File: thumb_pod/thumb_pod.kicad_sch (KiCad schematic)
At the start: 41 parts, among them J1 Conn_02x06_Odd_Even, J2 Conn_02x06_Odd_Even, J3 Conn_02x06_Odd_Even, SW1 SW_Push, SW10 SW_Push, SW2 SW_Push, SW3 SW_Push, SW4 SW_Push, SW5 SW_Push, SW6 SW_Push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

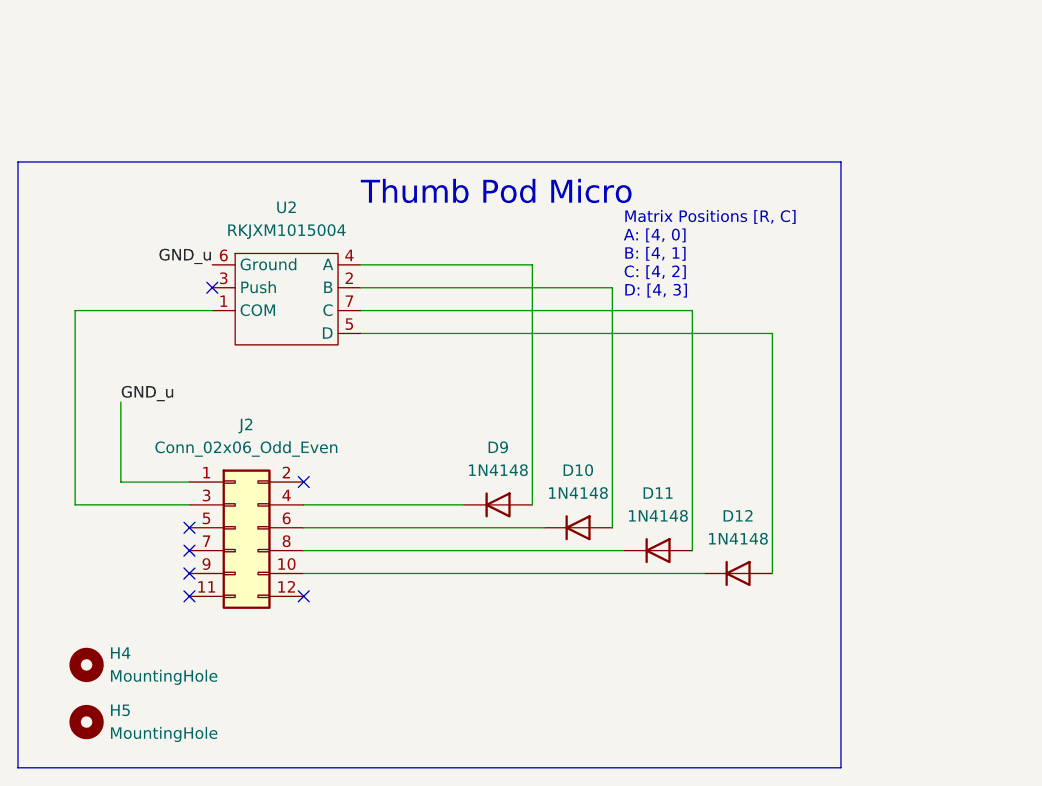
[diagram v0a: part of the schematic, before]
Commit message: - Removed "micro" thumb pod  - Added kailh gm microswitch footprint  - Switch to kail gm microswitches for the "mini" thumb pod  - Reduced size of joystick silkscreen
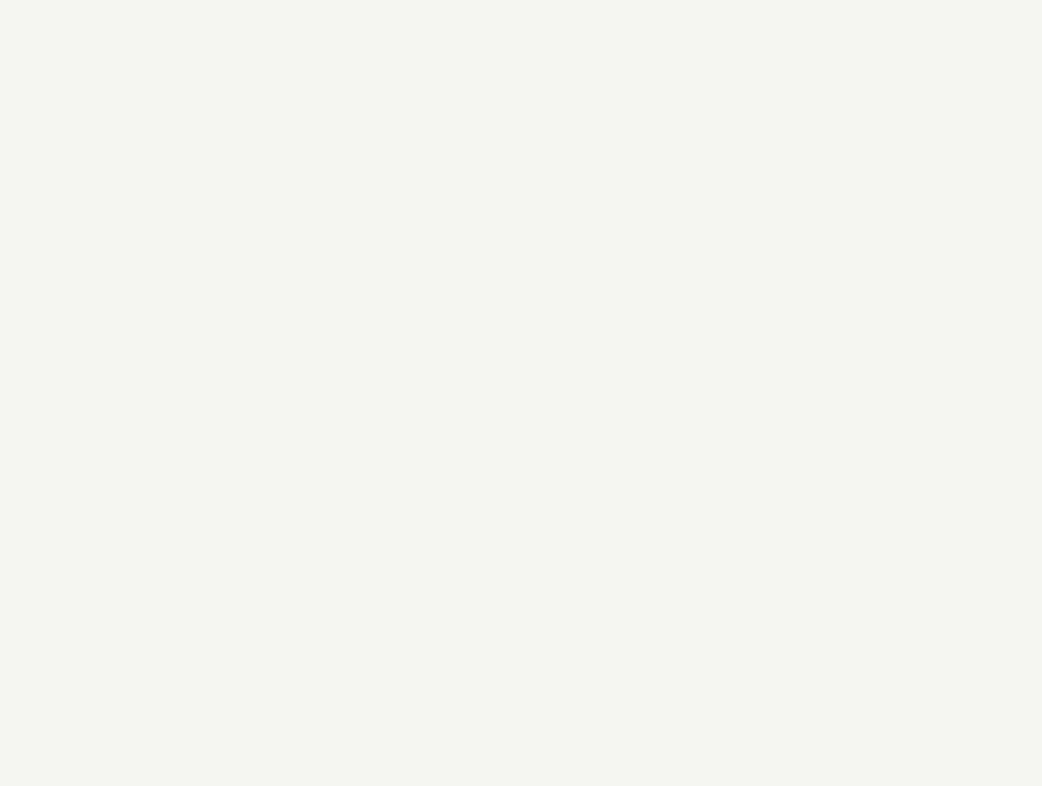
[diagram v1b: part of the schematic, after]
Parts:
- removed D10, D11, D12, D9: 1N4148, Diode_THT:D_DO-35_SOD27_P7.62mm_Horizontal, symbol Diode:1N4148
- removed H4, H5: MountingHole, MountingHole:MountingHole_3.2mm_M3, symbol Mechanical:MountingHole
- removed J2: Conn_02x06_Odd_Even, keypad:PinHeader_2x06_P2.54mm_Horizontal, symbol Connector_Generic:Conn_02x06_Odd_Even
- removed U2: RKJXM1015004, thumb_pod:RKJXM1015004, symbol thumb_pod:RKJXM1015004
- SW10, SW9: footprint Button_Switch_THT:SW_PUSH_6mm -> keypad:kailh_gm_microswitch
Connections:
- no-connect marks 19 -> 12
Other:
- note removed: "Matrix Positions [R, C] A: [4, 0] B: [4, 1] C: [4, 2] D: [4, 3]"
- note removed: "Thumb Pod Micro"

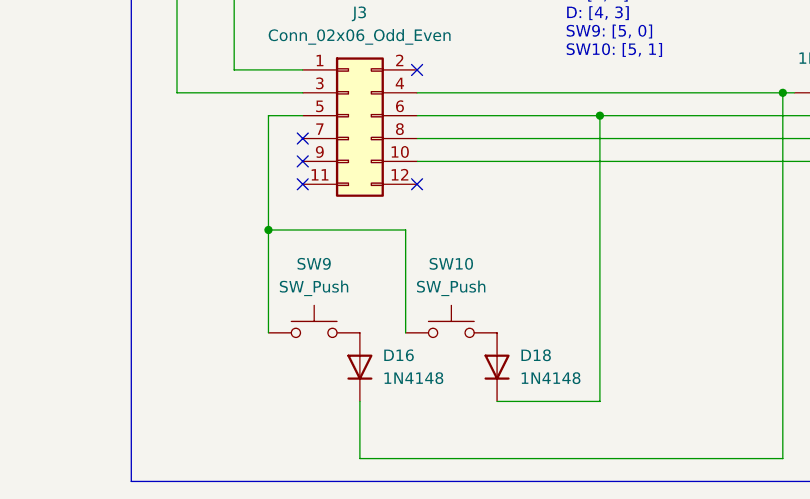
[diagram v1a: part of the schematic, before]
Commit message: - Updated the kailh gm switch footprint to match the SPDT symbol  - Updated the mini thumb pod switches to allow them to be placed in either orientation
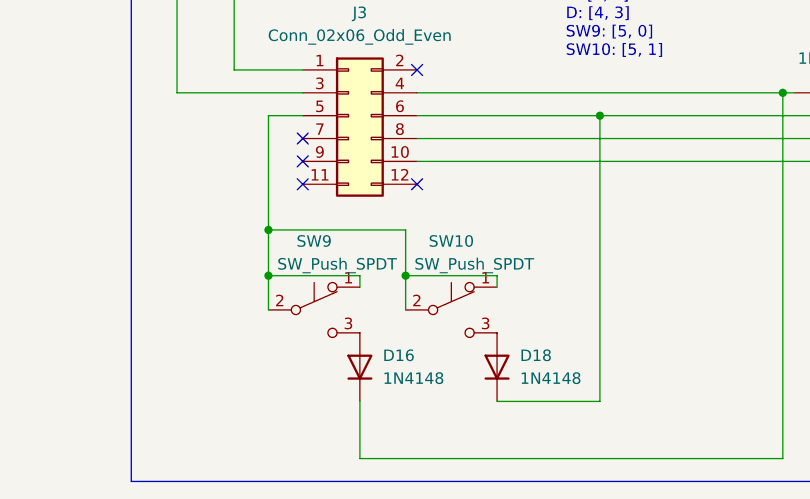
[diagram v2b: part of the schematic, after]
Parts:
- removed SW10, SW9: SW_Push, keypad:kailh_gm_microswitch, symbol Switch:SW_Push
- added SW10, SW9: SW_Push_SPDT, keypad:kailh_gm_microswitch, symbol Switch:SW_Push_SPDT
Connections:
- net at D18.2 (A): now also SW10.3 (C)
- net at J3.5 (Pin_5): now also SW10.1 (A), SW10.2 (B), SW9.1 (A), SW9.2 (B)
- net at D16.2 (A): now also SW9.3 (C)
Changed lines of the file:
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@@
   (junction (at 91.44 80.01) (diameter 0) (color 0 0 0 0)
+  )
+  (junction (at 182.88 138.43) (diameter 0) (color 0 0 0 0)
+  )
+  (junction (at 167.64 138.43) (diameter 0) (color 0 0 0 0)
   )
   (junction (at 71.12 90.17) (diameter 0) (color 0 0 0 0)
@@
     (stroke (width 0) (type default) (color 0 0 0 0))
   )
+  (wire (pts (xy 167.64 138.43) (xy 167.64 142.24))
+    (stroke (width 0) (type default) (color 0 0 0 0))
+  )
   (wire (pts (xy 116.84 80.01) (xy 116.84 90.17))
     (stroke (width 0) (type default) (color 0 0 0 0))
@@
     (stroke (width 0) (type default) (color 0 0 0 0))
   )
-  (wire (pts (xy 167.64 133.35) (xy 167.64 144.78))
+  (wire (pts (xy 167.64 133.35) (xy 167.64 138.43))
     (stroke (width 0) (type default) (color 0 0 0 0))
   )
@@
     (stroke (width 0) (type default) (color 0 0 0 0))
   )
+  (wire (pts (xy 177.8 139.7) (xy 177.8 138.43))
+    (stroke (width 0) (type default) (color 0 0 0 0))
+  )
   (wire (pts (xy 106.68 68.58) (xy 137.16 68.58))
     (stroke (width 0) (type default) (color 0 0 0 0))
@@
     (stroke (width 0) (type default) (color 0 0 0 0))
   )
+  (wire (pts (xy 182.88 138.43) (xy 182.88 142.24))
+    (stroke (width 0) (type default) (color 0 0 0 0))
+  )
+  (wire (pts (xy 167.64 138.43) (xy 177.8 138.43))
+    (stroke (width 0) (type default) (color 0 0 0 0))
+  )
   (wire (pts (xy 184.15 123.19) (xy 257.81 123.19))
     (stroke (width 0) (type default) (color 0 0 0 0))
@@
     (stroke (width 0) (type default) (color 0 0 0 0))
   )
+  (wire (pts (xy 182.88 138.43) (xy 193.04 138.43))
+    (stroke (width 0) (type default) (color 0 0 0 0))
+  )
   (wire (pts (xy 67.31 21.59) (xy 67.31 58.42))
     (stroke (width 0) (type default) (color 0 0 0 0))
@@
     (stroke (width 0) (type default) (color 0 0 0 0))
   )
-  (wire (pts (xy 182.88 133.35) (xy 182.88 144.78))
+  (wire (pts (xy 182.88 133.35) (xy 182.88 138.43))
     (stroke (width 0) (type default) (color 0 0 0 0))
   )
@@
   )
   (wire (pts (xy 99.06 26.67) (xy 99.06 58.42))
+    (stroke (width 0) (type default) (color 0 0 0 0))
+  )
+  (wire (pts (xy 193.04 139.7) (xy 193.04 138.43))
     (stroke (width 0) (type default) (color 0 0 0 0))
   )
@@
     (pin "2")
   )
-  (symbol (lib_id "Switch:SW_Push") (at 187.96 144.78 0) (unit 1)
-    (in_bom yes) (on_board yes) (fields_autoplaced)
-    (property "Reference" "SW10" (id 0) (at 187.96 137.16 0))
-    (property "Value" "SW_Push" (id 1) (at 187.96 139.7 0))
-    (property "Footprint" "keypad:kailh_gm_microswitch" (id 2) (at 187.96 139.7 0)
-      (effects (font (size 1.27 1.27)) hide)
-    )
-    (property "Datasheet" "~" (id 3) (at 187.96 139.7 0)
-      (effects (font (size 1.27 1.27)) hide)
-    )
-    (pin "1")
-    (pin "2")
-  )
   (symbol (lib_id "Switch:SW_Push") (at 96.52 80.01 0) (unit 1)
     (in_bom yes) (on_board yes) (fields_autoplaced)
@@
     )
     (property "Datasheet" "https://assets.nexperia.com/documents/data-sheet/1N4148_1N4448.pdf" (id 3) (at 110.49 99.06 0)
-      (effects (font (size 1.27 1.27)) hide)
-    )
-    (pin "1")
-    (pin "2")
-  )
-  (symbol (lib_id "Switch:SW_Push") (at 172.72 144.78 0) (unit 1)
-    (in_bom yes) (on_board yes) (fields_autoplaced)
-    (property "Reference" "SW9" (id 0) (at 172.72 137.16 0))
-    (property "Value" "SW_Push" (id 1) (at 172.72 139.7 0))
-    (property "Footprint" "keypad:kailh_gm_microswitch" (id 2) (at 172.72 139.7 0)
-      (effects (font (size 1.27 1.27)) hide)
-    )
-    (property "Datasheet" "~" (id 3) (at 172.72 139.7 0)
       (effects (font (size 1.27 1.27)) hide)
     )
@@
     (pin "2")
   )
+  (symbol (lib_id "Switch:SW_Push_SPDT") (at 172.72 142.24 0) (unit 1)
+    (in_bom yes) (on_board yes)
+    (property "Reference" "SW9" (id 0) (at 172.72 134.62 0))
+    (property "Value" "SW_Push_SPDT" (id 1) (at 175.26 137.16 0))
+    (property "Footprint" "keypad:kailh_gm_microswitch" (id 2) (at 172.72 142.24 0)
+      (effects (font (size 1.27 1.27)) hide)
+    )
+    (property "Datasheet" "~" (id 3) (at 172.72 142.24 0)
+      (effects (font (size 1.27 1.27)) hide)
+    )
+    (pin "1")
+    (pin "2")
+    (pin "3")
+  )
   (symbol (lib_name "1N4148_17") (lib_id "Diode:1N4148") (at 177.8 148.59 90) (unit 1)
     (in_bom yes) (on_board yes) (fields_autoplaced)
@@
     (pin "1")
     (pin "2")
+  )
+  (symbol (lib_id "Switch:SW_Push_SPDT") (at 187.96 142.24 0) (unit 1)
+    (in_bom yes) (on_board yes)
+    (property "Reference" "SW10" (id 0) (at 187.96 134.62 0))
+    (property "Value" "SW_Push_SPDT" (id 1) (at 190.5 137.16 0))
+    (property "Footprint" "keypad:kailh_gm_microswitch" (id 2) (at 187.96 142.24 0)
+      (effects (font (size 1.27 1.27)) hide)
+    )
+    (property "Datasheet" "~" (id 3) (at 187.96 142.24 0)
+      (effects (font (size 1.27 1.27)) hide)
+    )
+    (pin "1")
+    (pin "2")
+    (pin "3")
   )
   (symbol (lib_name "1N4148_13") (lib_id "Diode:1N4148") (at 80.01 99.06 0) (unit 1)
@@
       (reference "SW8") (unit 1) (value "SW_Push") (footprint "keypad:MXOnly-1U-Hotswap")
     )
-    (path "/87c90ff7-0ff8-4ee3-aefc-8735e4f5d617"
-      (reference "SW9") (unit 1) (value "SW_Push") (footprint "keypad:kailh_gm_microswitch")
-    )
-    (path "/60fbeb69-cf25-4af9-b8eb-9a90acbbc82e"
-      (reference "SW10") (unit 1) (value "SW_Push") (footprint "keypad:kailh_gm_microswitch")
+    (path "/d5cd553c-5877-4558-a639-d589f4be1c0e"
+      (reference "SW9") (unit 1) (value "SW_Push_SPDT") (footprint "keypad:kailh_gm_microswitch")
+    )
+    (path "/e646b8e1-128f-4252-852a-e97ceb233548"
+      (reference "SW10") (unit 1) (value "SW_Push_SPDT") (footprint "keypad:kailh_gm_microswitch")
     )
     (path "/ed67ef93-10f8-463e-9241-4d611de16424"

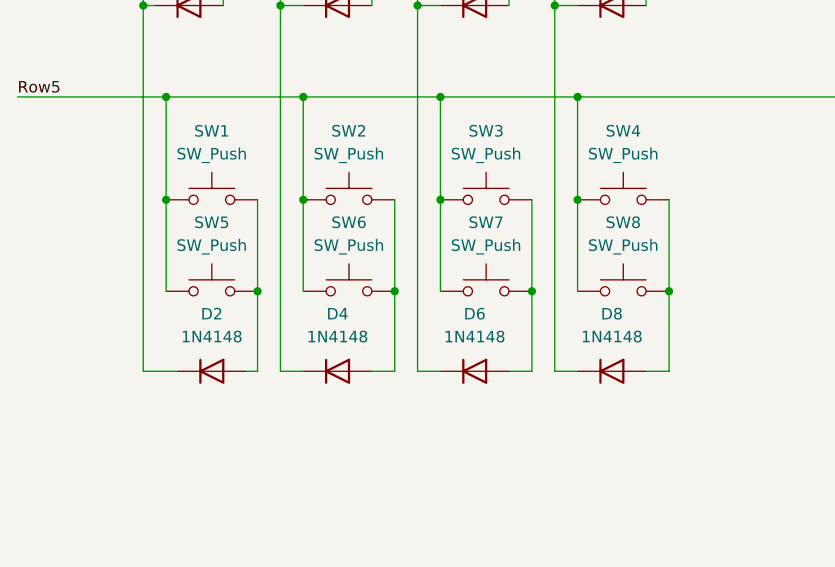
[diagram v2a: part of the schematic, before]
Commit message: - Abandoned the multi-position 1U switch experiment   - Added a notch to the thumb pod (normal sized)   - Adjusted button placement on the larger thumb pod based on testing   - Updated the readme
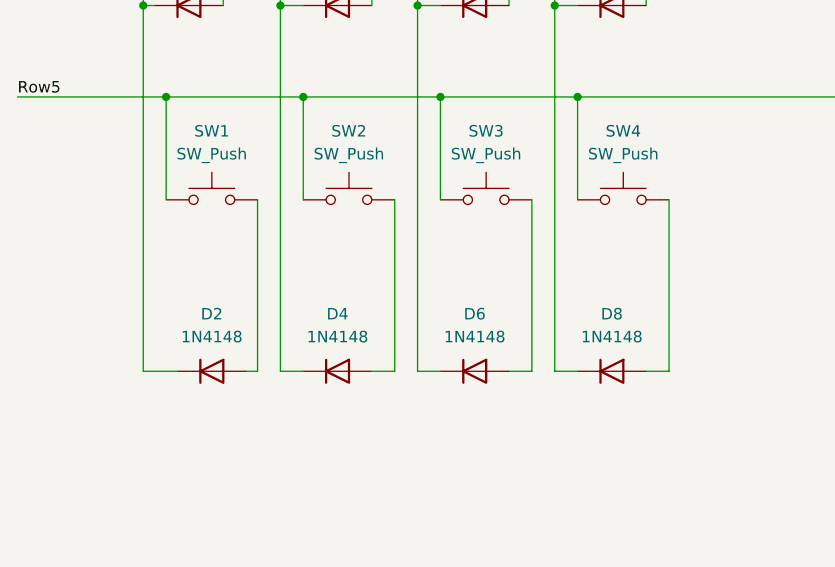
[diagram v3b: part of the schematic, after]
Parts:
- removed SW5, SW6, SW7, SW8: SW_Push, keypad:MXOnly-1U-Hotswap, symbol Switch:SW_Push
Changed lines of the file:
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@@
   (junction (at 91.44 68.58) (diameter 0) (color 0 0 0 0)
   )
-  (junction (at 101.6 90.17) (diameter 0) (color 0 0 0 0)
-  )
-  (junction (at 76.2 80.01) (diameter 0) (color 0 0 0 0)
-  )
   (junction (at 167.64 133.35) (diameter 0) (color 0 0 0 0)
   )
   (junction (at 73.66 58.42) (diameter 0) (color 0 0 0 0)
   )
-  (junction (at 86.36 90.17) (diameter 0) (color 0 0 0 0)
-  )
   (junction (at 224.79 118.11) (diameter 0) (color 0 0 0 0)
   )
@@
   (junction (at 58.42 58.42) (diameter 0) (color 0 0 0 0)
   )
-  (junction (at 116.84 90.17) (diameter 0) (color 0 0 0 0)
-  )
   (junction (at 106.68 68.58) (diameter 0) (color 0 0 0 0)
   )
@@
   (junction (at 104.14 58.42) (diameter 0) (color 0 0 0 0)
   )
-  (junction (at 106.68 80.01) (diameter 0) (color 0 0 0 0)
-  )
-  (junction (at 60.96 80.01) (diameter 0) (color 0 0 0 0)
-  )
-  (junction (at 91.44 80.01) (diameter 0) (color 0 0 0 0)
-  )
   (junction (at 182.88 138.43) (diameter 0) (color 0 0 0 0)
   )
   (junction (at 167.64 138.43) (diameter 0) (color 0 0 0 0)
-  )
-  (junction (at 71.12 90.17) (diameter 0) (color 0 0 0 0)
   )
   (no_connect (at 156.21 17.78))
@@
     (stroke (width 0) (type default) (color 0 0 0 0))
   )
-  (wire (pts (xy 101.6 90.17) (xy 101.6 99.06))
+  (wire (pts (xy 101.6 80.01) (xy 101.6 99.06))
     (stroke (width 0) (type default) (color 0 0 0 0))
   )
@@
     (stroke (width 0) (type default) (color 0 0 0 0))
   )
-  (wire (pts (xy 116.84 80.01) (xy 116.84 90.17))
+  (wire (pts (xy 116.84 80.01) (xy 116.84 99.06))
     (stroke (width 0) (type default) (color 0 0 0 0))
   )
@@
     (stroke (width 0) (type default) (color 0 0 0 0))
   )
-  (wire (pts (xy 106.68 80.01) (xy 106.68 90.17))
-    (stroke (width 0) (type default) (color 0 0 0 0))
-  )
   (wire (pts (xy 214.63 88.9) (xy 233.68 88.9))
     (stroke (width 0) (type default) (color 0 0 0 0))
@@
     (stroke (width 0) (type default) (color 0 0 0 0))
   )
-  (wire (pts (xy 86.36 90.17) (xy 86.36 99.06))
-    (stroke (width 0) (type default) (color 0 0 0 0))
-  )
   (wire (pts (xy 104.14 58.42) (xy 104.14 99.06))
     (stroke (width 0) (type default) (color 0 0 0 0))
@@
     (stroke (width 0) (type default) (color 0 0 0 0))
   )
-  (wire (pts (xy 116.84 90.17) (xy 116.84 99.06))
-    (stroke (width 0) (type default) (color 0 0 0 0))
-  )
   (polyline (pts (xy 152.4 161.29) (xy 152.4 78.74))
     (stroke (width 0) (type default) (color 0 0 0 0))
@@
     (stroke (width 0) (type default) (color 0 0 0 0))
   )
-  (wire (pts (xy 101.6 80.01) (xy 101.6 90.17))
-    (stroke (width 0) (type default) (color 0 0 0 0))
-  )
   (wire (pts (xy 265.43 93.98) (xy 265.43 123.19))
     (stroke (width 0) (type default) (color 0 0 0 0))
   )
-  (wire (pts (xy 71.12 90.17) (xy 71.12 99.06))
-    (stroke (width 0) (type default) (color 0 0 0 0))
-  )
   (wire (pts (xy 182.88 138.43) (xy 193.04 138.43))
     (stroke (width 0) (type default) (color 0 0 0 0))
@@
     (stroke (width 0) (type default) (color 0 0 0 0))
   )
-  (wire (pts (xy 86.36 80.01) (xy 86.36 90.17))
+  (wire (pts (xy 86.36 80.01) (xy 86.36 99.06))
     (stroke (width 0) (type default) (color 0 0 0 0))
   )
@@
     (stroke (width 0) (type default) (color 0 0 0 0))
   )
-  (wire (pts (xy 91.44 80.01) (xy 91.44 90.17))
-    (stroke (width 0) (type default) (color 0 0 0 0))
-  )
   (wire (pts (xy 149.86 34.29) (xy 157.48 34.29))
     (stroke (width 0) (type default) (color 0 0 0 0))
@@
     (stroke (width 0) (type default) (color 0 0 0 0))
   )
-  (wire (pts (xy 76.2 80.01) (xy 76.2 90.17))
-    (stroke (width 0) (type default) (color 0 0 0 0))
-  )
   (wire (pts (xy 73.66 58.42) (xy 73.66 99.06))
     (stroke (width 0) (type default) (color 0 0 0 0))
@@
     (stroke (width 0) (type default) (color 0 0 0 0))
   )
-  (wire (pts (xy 71.12 80.01) (xy 71.12 90.17))
+  (wire (pts (xy 71.12 80.01) (xy 71.12 99.06))
     (stroke (width 0) (type default) (color 0 0 0 0))
   )
   (wire (pts (xy 58.42 58.42) (xy 59.69 58.42))
-    (stroke (width 0) (type default) (color 0 0 0 0))
-  )
-  (wire (pts (xy 60.96 80.01) (xy 60.96 90.17))
     (stroke (width 0) (type default) (color 0 0 0 0))
   )
@@
     (pin "2")
   )
-  (symbol (lib_id "Switch:SW_Push") (at 66.04 90.17 0) (unit 1)
-    (in_bom no) (on_board yes) (fields_autoplaced)
-    (property "Reference" "SW5" (id 0) (at 66.04 82.55 0))
-    (property "Value" "SW_Push" (id 1) (at 66.04 85.09 0))
-    (property "Footprint" "keypad:MXOnly-1U-Hotswap" (id 2) (at 66.04 85.09 0)
-      (effects (font (size 1.27 1.27)) hide)
-    )
-    (property "Datasheet" "~" (id 3) (at 66.04 85.09 0)
-      (effects (font (size 1.27 1.27)) hide)
-    )
-    (pin "1")
-    (pin "2")
-  )
   (symbol (lib_id "Switch:SW_Push") (at 111.76 80.01 0) (unit 1)
     (in_bom yes) (on_board yes) (fields_autoplaced)
@@
     (pin "2")
   )
-  (symbol (lib_id "Switch:SW_Push") (at 111.76 90.17 0) (unit 1)
-    (in_bom no) (on_board yes) (fields_autoplaced)
-    (property "Reference" "SW8" (id 0) (at 111.76 82.55 0))
-    (property "Value" "SW_Push" (id 1) (at 111.76 85.09 0))
-    (property "Footprint" "keypad:MXOnly-1U-Hotswap" (id 2) (at 111.76 85.09 0)
-      (effects (font (size 1.27 1.27)) hide)
-    )
-    (property "Datasheet" "~" (id 3) (at 111.76 85.09 0)
-      (effects (font (size 1.27 1.27)) hide)
-    )
-    (pin "1")
-    (pin "2")
-  )
   (symbol (lib_name "1N4148_16") (lib_id "Diode:1N4148") (at 261.62 123.19 0) (unit 1)
     (in_bom yes) (on_board yes) (fields_autoplaced)
@@
     )
     (property "Datasheet" "https://assets.nexperia.com/documents/data-sheet/1N4148_1N4448.pdf" (id 3) (at 276.86 125.73 0)
-      (effects (font (size 1.27 1.27)) hide)
-    )
-    (pin "1")
-    (pin "2")
-  )
-  (symbol (lib_id "Switch:SW_Push") (at 96.52 90.17 0) (unit 1)
-    (in_bom no) (on_board yes) (fields_autoplaced)
-    (property "Reference" "SW7" (id 0) (at 96.52 82.55 0))
-    (property "Value" "SW_Push" (id 1) (at 96.52 85.09 0))
-    (property "Footprint" "keypad:MXOnly-1U-Hotswap" (id 2) (at 96.52 85.09 0)
-      (effects (font (size 1.27 1.27)) hide)
-    )
-    (property "Datasheet" "~" (id 3) (at 96.52 85.09 0)
       (effects (font (size 1.27 1.27)) hide)
     )
@@
     (pin "7")
   )
-  (symbol (lib_id "Switch:SW_Push") (at 81.28 90.17 0) (unit 1)
-    (in_bom no) (on_board yes) (fields_autoplaced)
-    (property "Reference" "SW6" (id 0) (at 81.28 82.55 0))
-    (property "Value" "SW_Push" (id 1) (at 81.28 85.09 0))
-    (property "Footprint" "keypad:MXOnly-1U-Hotswap" (id 2) (at 81.28 85.09 0)
-      (effects (font (size 1.27 1.27)) hide)
-    )
-    (property "Datasheet" "~" (id 3) (at 81.28 85.09 0)
-      (effects (font (size 1.27 1.27)) hide)
-    )
-    (pin "1")
-    (pin "2")
-  )
   (symbol (lib_id "Mechanical:MountingHole") (at 20.32 36.83 0) (unit 1)
     (in_bom yes) (on_board yes) (fields_autoplaced)
@@
       (reference "SW4") (unit 1) (value "SW_Push") (footprint "keypad:MXOnly-1U-Hotswap")
     )
-    (path "/4ef455b3-ba34-4232-bf2f-9149d79d138f"
-      (reference "SW5") (unit 1) (value "SW_Push") (footprint "keypad:MXOnly-1U-Hotswap")
-    )
-    (path "/f0174d25-fcae-40c2-9661-cfb60655dfee"
-      (reference "SW6") (unit 1) (value "SW_Push") (footprint "keypad:MXOnly-1U-Hotswap")
-    )
-    (path "/d08a55e9-ec41-4c13-a753-d90ce88434ee"
-      (reference "SW7") (unit 1) (value "SW_Push") (footprint "keypad:MXOnly-1U-Hotswap")
-    )
-    (path "/aed9d124-642d-428a-a54a-196b0a6d4104"
-      (reference "SW8") (unit 1) (value "SW_Push") (footprint "keypad:MXOnly-1U-Hotswap")
-    )
     (path "/d5cd553c-5877-4558-a639-d589f4be1c0e"

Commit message: - Split the thumb pod PCBs
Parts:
- removed D13, D14, D15, D16, D17, D18: 1N4148, Diode_THT:D_DO-35_SOD27_P7.62mm_Horizontal, symbol Diode:1N4148
- removed H6, H7: MountingHole, MountingHole:MountingHole_3.2mm_M3, symbol Mechanical:MountingHole
- removed J3: Conn_02x06_Odd_Even, keypad:PinHeader_2x06_P2.54mm_Horizontal, symbol Connector_Generic:Conn_02x06_Odd_Even
- removed SW10, SW9: SW_Push_SPDT, keypad:kailh_gm_microswitch, symbol Switch:SW_Push_SPDT
- removed U3: RKJXM1015004, thumb_pod:RKJXM1015004, symbol thumb_pod:RKJXM1015004
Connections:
- no-connect marks 12 -> 6
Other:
- note removed: "Matrix Positions [R, C] A: [4, 0] B: [4, 1] C: [4, 2] D: [4, 3] SW9: [5, 0] SW10: [5, 1]"
- note removed: "Thumb Pod Mini"
